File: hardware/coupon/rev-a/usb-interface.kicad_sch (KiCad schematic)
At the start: 20 parts, among them J1 USB4505-03-0-A, U29 TLV75533PDBVR, U30 BQ24392RSER, U31 TUSB320LAIRWBR, U32 TS3USB31ERSER, U33 TPD4E05U06DQAR

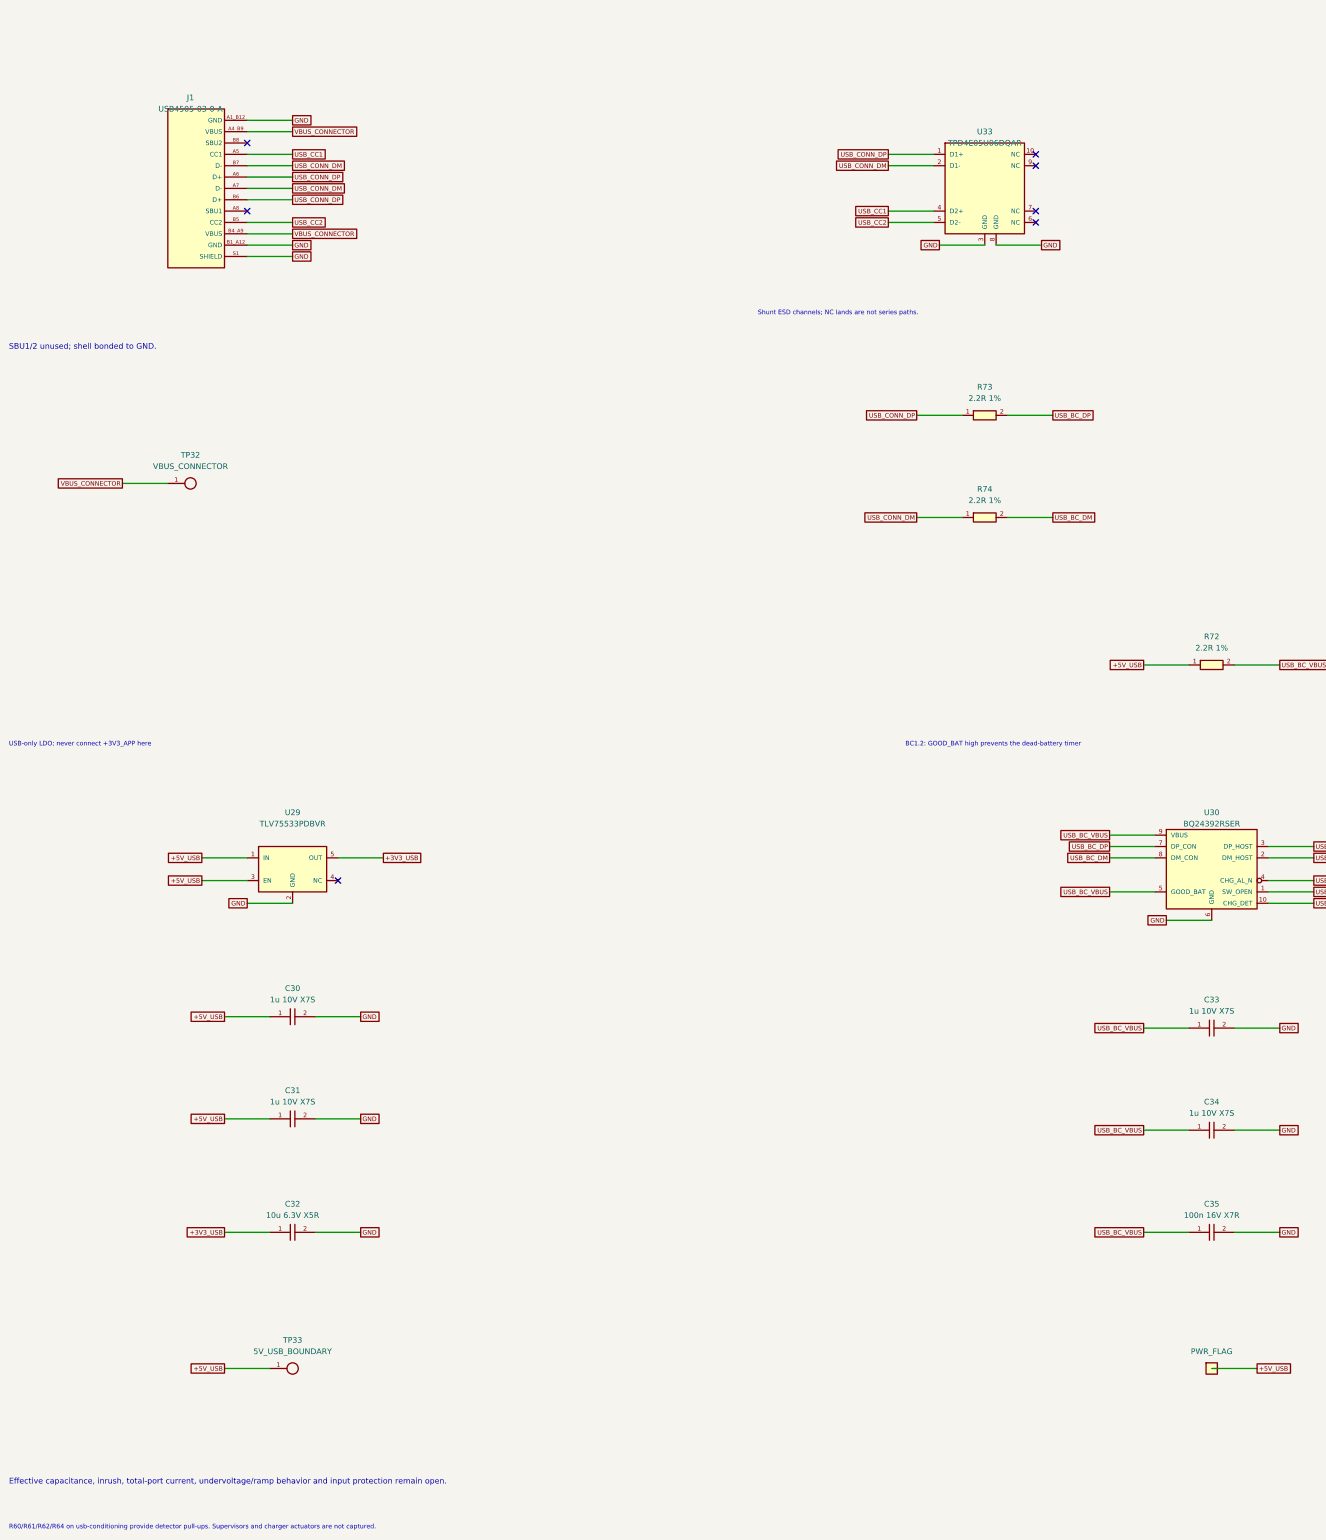
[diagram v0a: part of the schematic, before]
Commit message: Review native USB capture and add staged logic-rail supervision
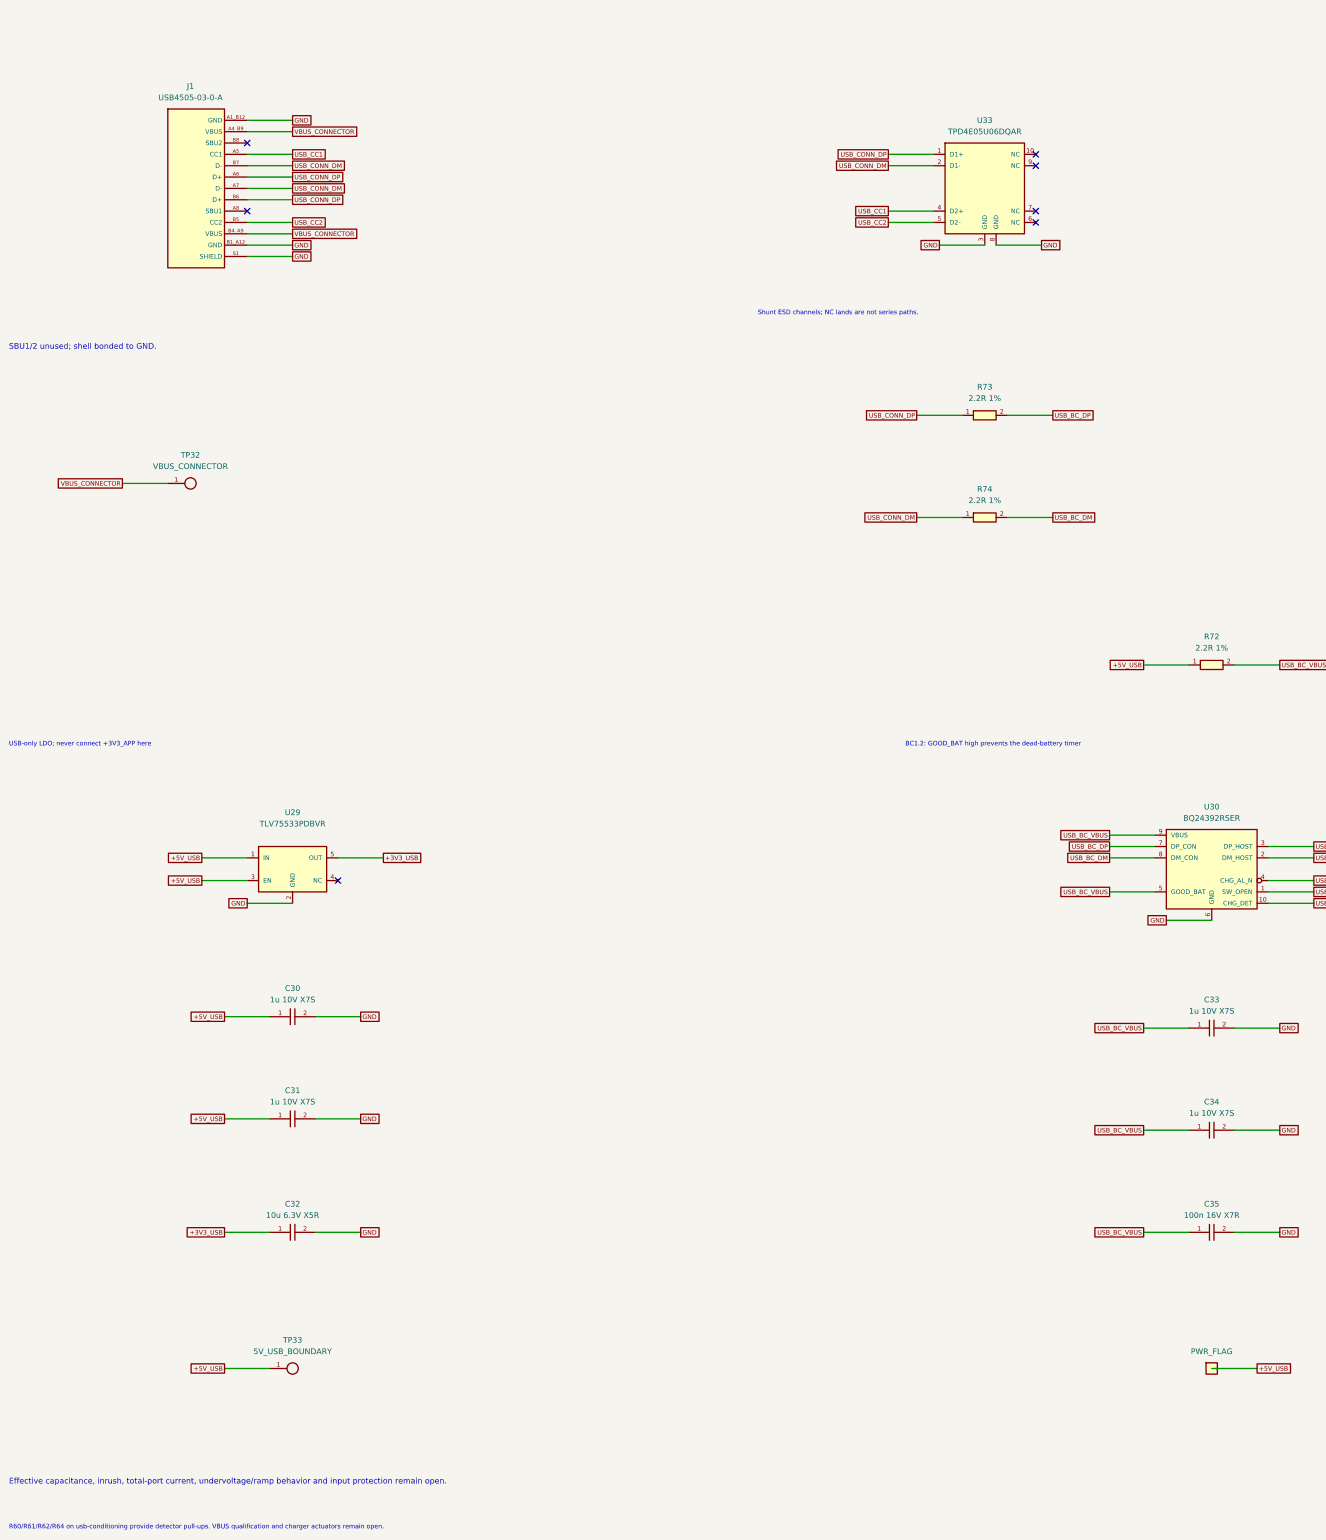
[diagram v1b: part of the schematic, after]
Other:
- note added: "R60/R61/R62/R64 on usb-conditioning provide detector pull-ups. VBUS qualification and charger actuators remain open."
- note removed: "R60/R61/R62/R64 on usb-conditioning provide detector pull-ups. Supervisors and charger actuators are not captured."
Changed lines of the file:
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@@
 (symbol (lib_id "rgb-badge-coupon:USB4505-03-0-A") (at 60.960 91.440 0) (unit 1)
 (exclude_from_sim no) (in_bom yes) (on_board yes) (dnp no)
-(property "Reference" "J1" (at 60.960 71.120 0) (effects (font (size 1.27 1.27))))
-(property "Value" "USB4505-03-0-A" (at 60.960 73.660 0) (effects (font (size 1.27 1.27))))
+(property "Reference" "J1" (at 60.960 68.580 0) (effects (font (size 1.27 1.27))))
+(property "Value" "USB4505-03-0-A" (at 60.960 71.120 0) (effects (font (size 1.27 1.27))))
 (property "Footprint" "rgb-badge-coupon:USB_C_GCT_USB4505-03-0-A_MidMount" (at 60.960 91.440 0) (effects (font (size 1.27 1.27)) (hide yes)))
 (property "Datasheet" "https://gct.co/files/drawings/usb4505.pdf" (at 60.960 91.440 0) (effects (font (size 1.27 1.27)) (hide yes)))
@@
 (symbol (lib_id "rgb-badge-coupon:TPD4E05U06DQAR") (at 238.760 91.440 0) (unit 1)
 (exclude_from_sim no) (in_bom yes) (on_board yes) (dnp no)
-(property "Reference" "U33" (at 238.760 78.740 0) (effects (font (size 1.27 1.27))))
-(property "Value" "TPD4E05U06DQAR" (at 238.760 81.280 0) (effects (font (size 1.27 1.27))))
+(property "Reference" "U33" (at 238.760 76.200 0) (effects (font (size 1.27 1.27))))
+(property "Value" "TPD4E05U06DQAR" (at 238.760 78.740 0) (effects (font (size 1.27 1.27))))
 (property "Footprint" "rgb-badge-coupon:USON_TI_DQA0010A" (at 238.760 91.440 0) (effects (font (size 1.27 1.27)) (hide yes)))
 (property "Datasheet" "https://www.ti.com/lit/ds/symlink/tpd4e05u06.pdf" (at 238.760 91.440 0) (effects (font (size 1.27 1.27)) (hide yes)))
@@
 (symbol (lib_id "rgb-badge-coupon:BQ24392RSER") (at 289.560 243.840 0) (unit 1)
 (exclude_from_sim no) (in_bom yes) (on_board yes) (dnp no)
-(property "Reference" "U30" (at 289.560 231.140 0) (effects (font (size 1.27 1.27))))
-(property "Value" "BQ24392RSER" (at 289.560 233.680 0) (effects (font (size 1.27 1.27))))
+(property "Reference" "U30" (at 289.560 229.870 0) (effects (font (size 1.27 1.27))))
+(property "Value" "BQ24392RSER" (at 289.560 232.410 0) (effects (font (size 1.27 1.27))))
 (property "Footprint" "rgb-badge-coupon:UQFN_TI_RSE0010A_2x1.5mm_P0.5mm" (at 289.560 243.840 0) (effects (font (size 1.27 1.27)) (hide yes)))
 (property "Datasheet" "https://www.ti.com/lit/ds/symlink/bq24392.pdf" (at 289.560 243.840 0) (effects (font (size 1.27 1.27)) (hide yes)))
@@
 (text "#FLG06: ERC power annotation after R72; not another source." (at 426.720 370.840 0) (effects (font (size 1.016 1.016)) (justify left)))
 (text "Effective capacitance, inrush, total-port current, undervoltage/ramp behavior and input protection remain open." (at 20.320 381.000 0) (effects (font (size 1.27 1.27)) (justify left)))
-(text "R60/R61/R62/R64 on usb-conditioning provide detector pull-ups. Supervisors and charger actuators are not captured." (at 20.320 391.160 0) (effects (font (size 1.016 1.016)) (justify left)))
+(text "R60/R61/R62/R64 on usb-conditioning provide detector pull-ups. VBUS qualification and charger actuators remain open." (at 20.320 391.160 0) (effects (font (size 1.016 1.016)) (justify left)))
 (embedded_fonts no)
 )

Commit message: Simplify charging to Type-C-only fixed-current policy
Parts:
- removed C33, C34: 1u 10V X7S, rgb-badge-coupon:C_Murata_GRM15_0402, symbol rgb-badge-coupon:GRM155C71A105KE11D
- removed C35: 100n 16V X7R, rgb-badge-coupon:C_Murata_GRM15_0402, symbol rgb-badge-coupon:GRM155R71C104KA88D
- removed R72, R73, R74: 2.2R 1%, rgb-badge-coupon:R_Panasonic_ERJ2_0402, symbol rgb-badge-coupon:ERJ-2RCF2R20X
- removed U30: BQ24392RSER, rgb-badge-coupon:UQFN_TI_RSE0010A_2x1.5mm_P0.5mm, symbol rgb-badge-coupon:BQ24392RSER
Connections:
- net USB_BC_HOST_DM is gone; now on net USB_CONN_DM: U32.5 (D-)
- net USB_BC_HOST_DP is gone; now on net USB_CONN_DP: U32.3 (D+)
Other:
- note added: "D pins face connector; HSD pins face ESP32."
- note added: "R60/R61 provide Type-C output pull-ups. USB-A/default-current sources: data only while ON, no charging."
- note added: "USB interface: connector, Type-C-only permission, switched data and USB-only logic supply"
- note removed: "#FLG06: ERC power annotation after R72; not another source."
- note removed: "BC1.2: GOOD_BAT high prevents the dead-battery timer"
- note removed: "D pins face detector; HSD pins face ESP32."
- note removed: "R60/R61/R62/R64 on usb-conditioning provide detector pull-ups. VBUS qualification and charger actuators remain open."
- note removed: "USB interface: connector, CC / BC1.2 detection, switched data and USB-only logic supply"
